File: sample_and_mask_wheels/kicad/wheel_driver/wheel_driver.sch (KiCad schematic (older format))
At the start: 10 parts, among them J1 Screw_Terminal_01x04, J2 Screw_Terminal_01x04, J3 Screw_Terminal_01x04, SW1 SW_Coded_SH-7040

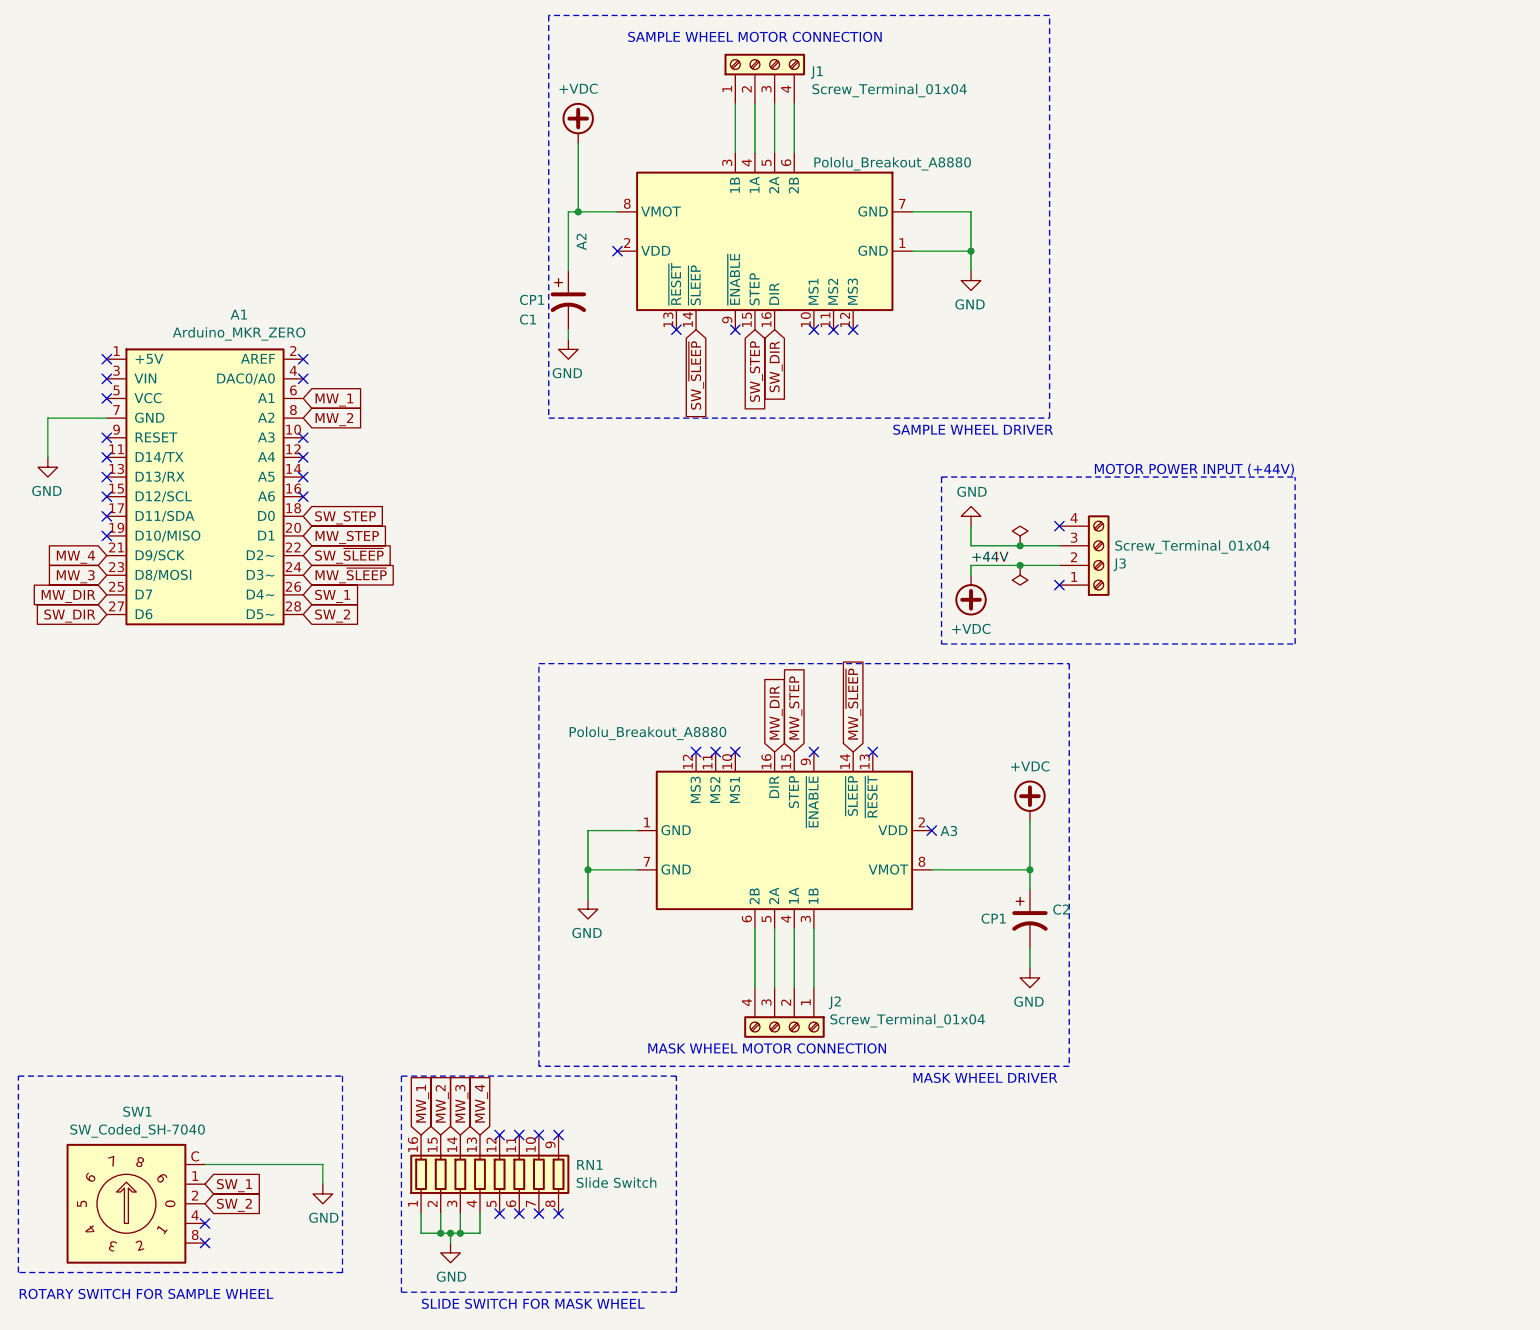
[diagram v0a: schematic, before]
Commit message: add motor connections to schematifc
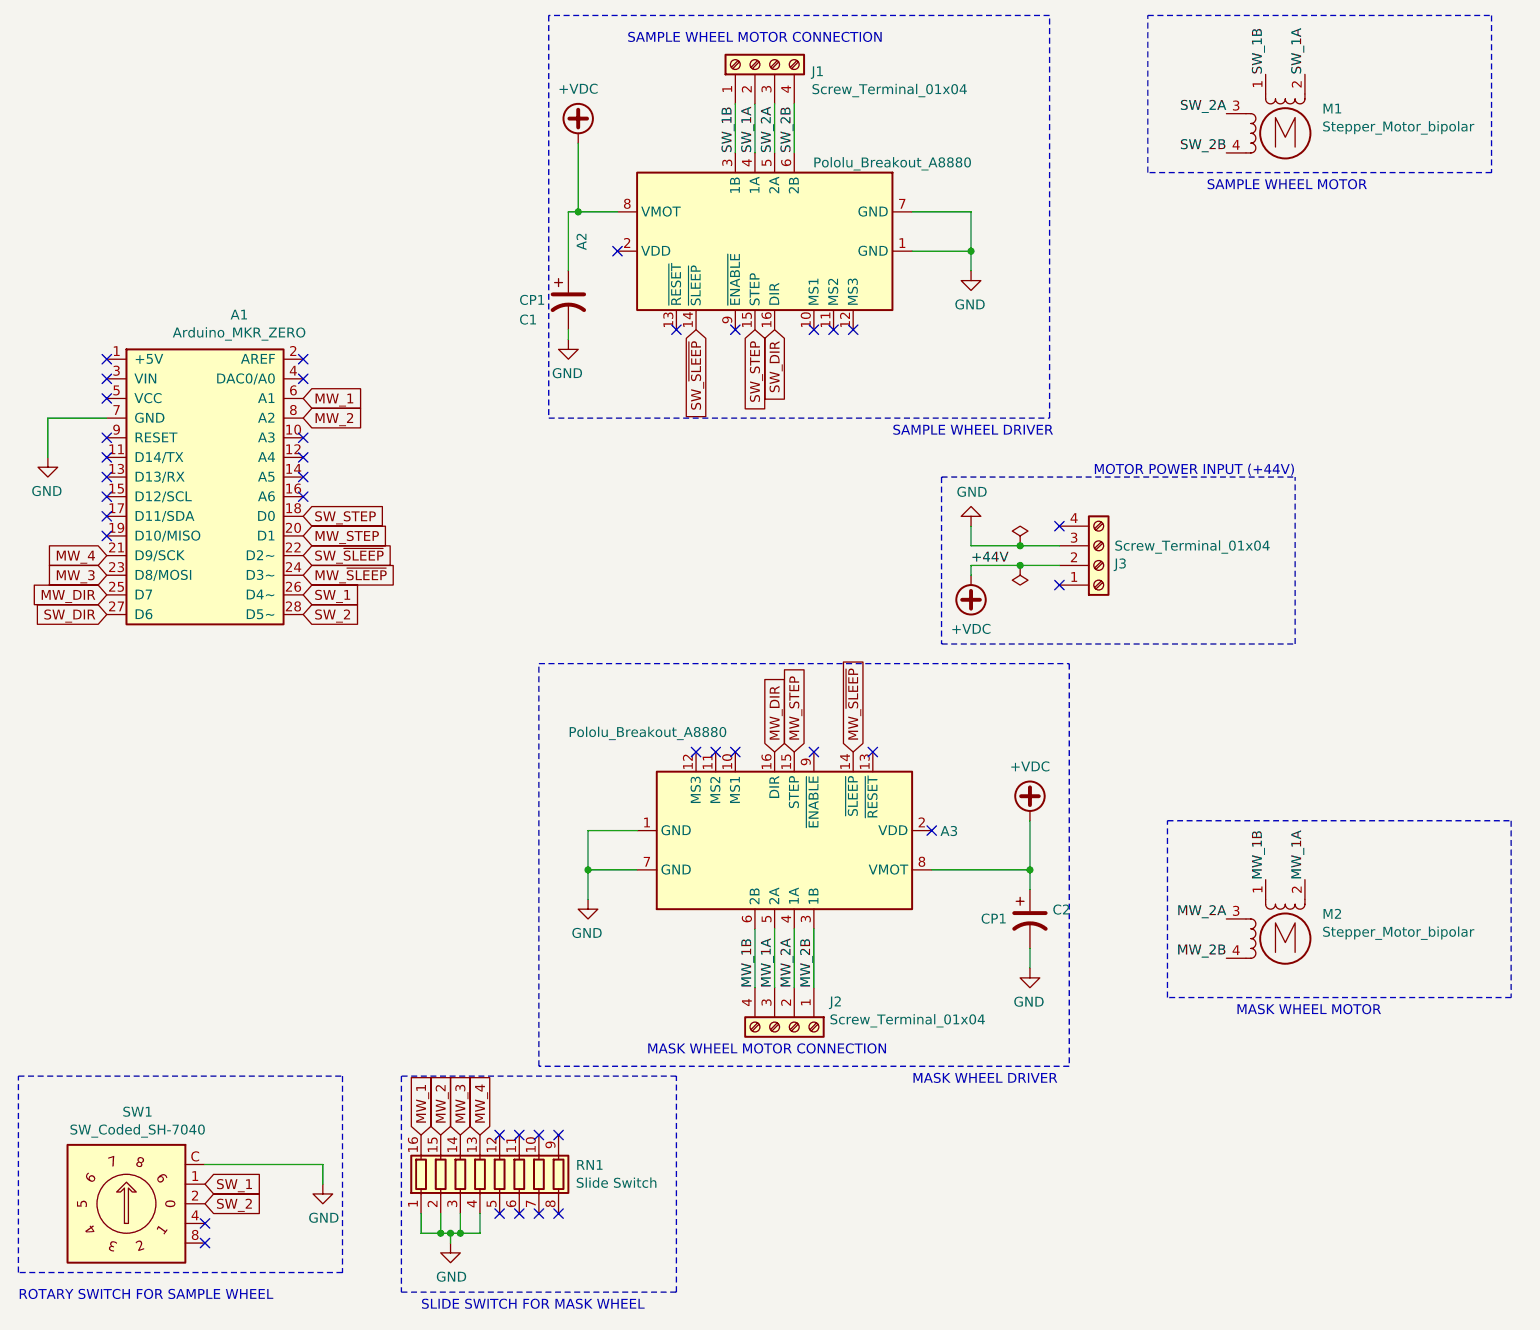
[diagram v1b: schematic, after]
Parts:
- added M1, M2: Stepper_Motor_bipolar, symbol Motor:Stepper_Motor_bipolar
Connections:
- net SW_1B: now reaches A2.3 (1B), J1.1 (Pin_1)
- net SW_1B: now also M1.1
- net SW_1A: now reaches A2.4 (1A), J1.2 (Pin_2)
- net SW_1A: now also M1.2 (-)
- net SW_2A: now reaches A2.5 (2A), J1.3 (Pin_3)
- net SW_2A: now also M1.3
- net SW_2B: now reaches A2.6 (2B), J1.4 (Pin_4)
- net SW_2B: now also M1.4
- net MW_2B: now reaches A3.3 (1B), J2.1 (Pin_1)
- net MW_2B: now also M2.4
- net MW_2A: now reaches A3.4 (1A), J2.2 (Pin_2)
- net MW_2A: now also M2.3
- net MW_1A: now reaches A3.5 (2A), J2.3 (Pin_3)
- net MW_1A: now also M2.2 (-)
- net MW_1B: now reaches A3.6 (2B), J2.4 (Pin_4)
- net MW_1B: now also M2.1
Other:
- note added: "MASK WHEEL MOTOR"
- note added: "SAMPLE WHEEL MOTOR"
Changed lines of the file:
@@
 EESchema Schematic File Version 4
+LIBS:wheel_driver-cache
 EELAYER 29 0
 EELAYER END
@@
 Wire Wire Line
 	6450 3400 6200 3400
+$Comp
+L Motor:Stepper_Motor_bipolar M1
+U 1 1 5BDB3F6A
+P 7800 1200
+F 0 "M1" H 7988 1324 50  0000 L CNN
+F 1 "Stepper_Motor_bipolar" H 7988 1233 50  0000 L CNN
+F 2 "" H 7810 1190 50  0001 C CNN
+F 3 "http://www.infineon.com/dgdl/Application-Note-TLE8110EE_driving_UniPolarStepperMotor_V1.1.pdf?fileId=db3a30431be39b97011be5d0aa0a00b0" H 7810 1190 50  0001 C CNN
+	1    7800 1200
+	1    0    0    -1
+$EndComp
+$Comp
+L Motor:Stepper_Motor_bipolar M2
+U 1 1 5BDB54BA
+P 7800 5300
+F 0 "M2" H 7988 5424 50  0000 L CNN
+F 1 "Stepper_Motor_bipolar" H 7988 5333 50  0000 L CNN
+F 2 "" H 7810 5290 50  0001 C CNN
+F 3 "http://www.infineon.com/dgdl/Application-Note-TLE8110EE_driving_UniPolarStepperMotor_V1.1.pdf?fileId=db3a30431be39b97011be5d0aa0a00b0" H 7810 5290 50  0001 C CNN
+	1    7800 5300
+	1    0    0    -1
+$EndComp
+Text Notes 7550 5700 0    50   ~ 0
+MASK WHEEL MOTOR
+Text Notes 7400 1500 0    50   ~ 0
+SAMPLE WHEEL MOTOR
+Text Label 5300 1300 1    50   ~ 0
+SW_2B
+Text Label 5200 1300 1    50   ~ 0
+SW_2A
+Text Label 5100 1300 1    50   ~ 0
+SW_1A
+Text Label 5000 1300 1    50   ~ 0
+SW_1B
+Text Label 7500 1300 2    50   ~ 0
+SW_2B
+Text Label 7500 1100 2    50   ~ 0
+SW_2A
+Text Label 7700 900  1    50   ~ 0
+SW_1B
+Text Label 7900 900  1    50   ~ 0
+SW_1A
+Wire Notes Line
+	7100 600  8850 600
+Wire Notes Line
+	8850 600  8850 1400
+Wire Notes Line
+	8850 1400 7100 1400
+Wire Notes Line
+	7100 1400 7100 600
+Text Label 5100 5550 1    50   ~ 0
+MW_1B
+Text Label 5200 5550 1    50   ~ 0
+MW_1A
+Text Label 5300 5550 1    50   ~ 0
+MW_2A
+Text Label 5400 5550 1    50   ~ 0
+MW_2B
+Text Label 7700 5000 1    50   ~ 0
+MW_1B
+Text Label 7900 5000 1    50   ~ 0
+MW_1A
+Text Label 7500 5200 2    50   ~ 0
+MW_2A
+Text Label 7500 5400 2    50   ~ 0
+MW_2B
+Wire Notes Line
+	7200 5600 7200 4700
+Wire Notes Line
+	7200 4700 8950 4700
+Wire Notes Line
+	8950 4700 8950 5600
+Wire Notes Line
+	8950 5600 7200 5600
 $EndSCHEMATC

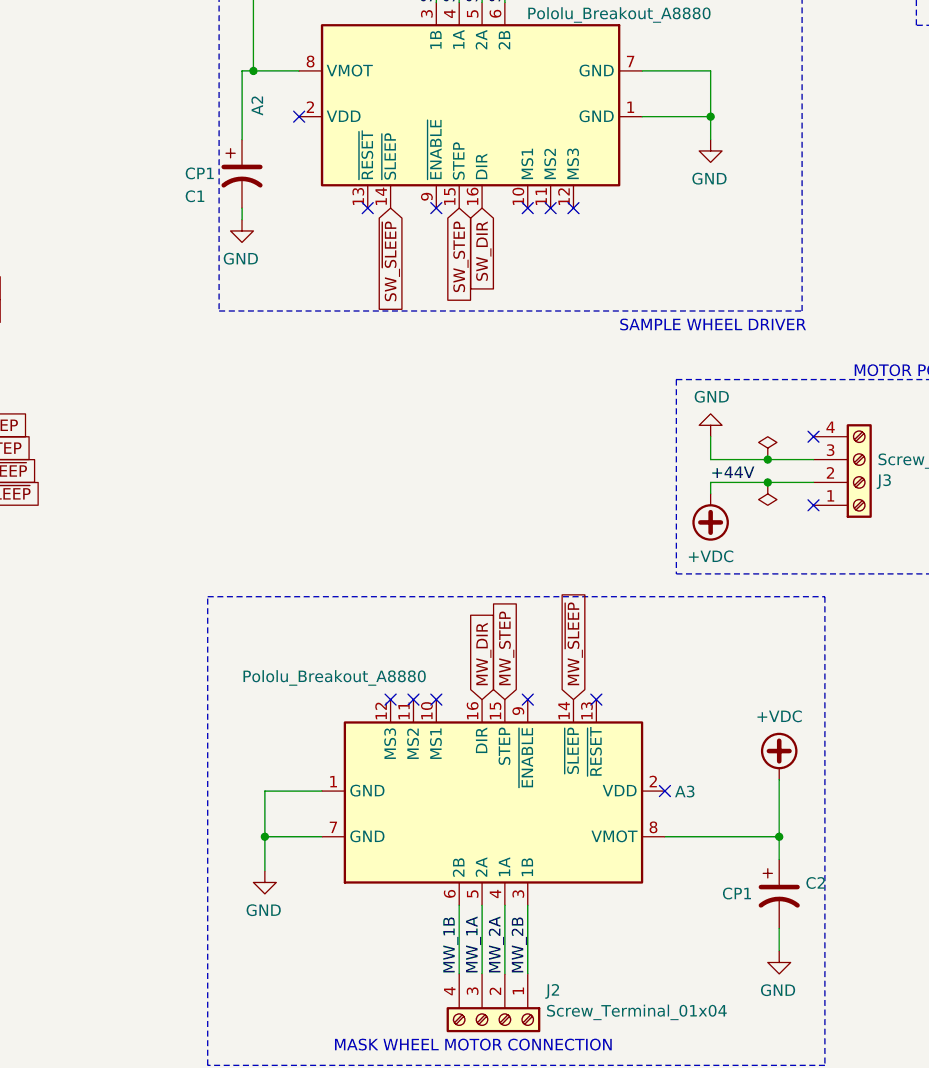
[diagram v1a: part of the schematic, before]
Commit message: fix cap value in schemtaic
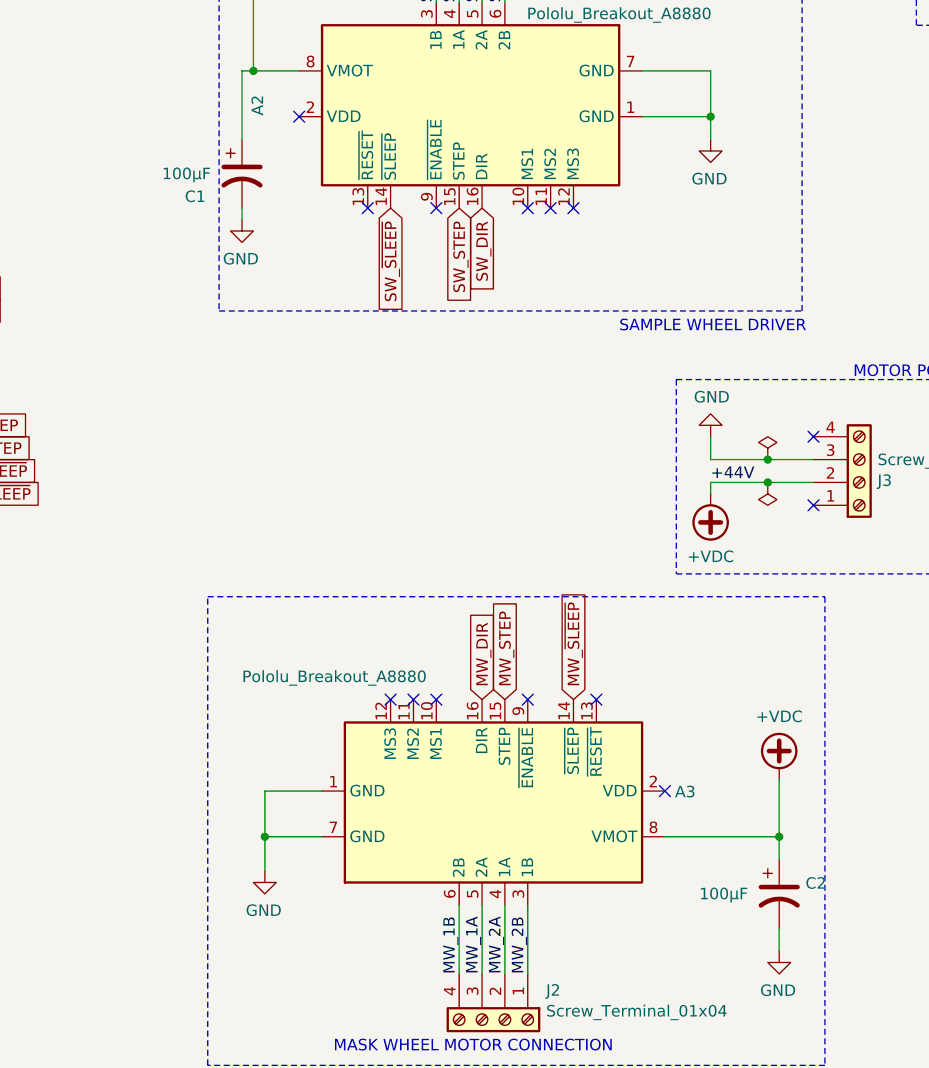
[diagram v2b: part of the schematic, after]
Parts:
- C1, C2: value CP1 -> 100μF
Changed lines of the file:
@@
 P 4150 2050
 F 0 "C1" H 3900 1950 50  0000 L CNN
-F 1 "CP1" H 3900 2050 50  0000 L CNN
+F 1 "100μF" H 3800 2050 50  0000 L CNN
 F 2 "" H 4150 2050 50  0001 C CNN
 F 3 "~" H 4150 2050 50  0001 C CNN
@@
 P 6500 5200
 F 0 "C2" H 6615 5246 50  0000 L CNN
-F 1 "CP1" H 6250 5200 50  0000 L CNN
+F 1 "100μF" H 6150 5200 50  0000 L CNN
 F 2 "" H 6500 5200 50  0001 C CNN
 F 3 "~" H 6500 5200 50  0001 C CNN

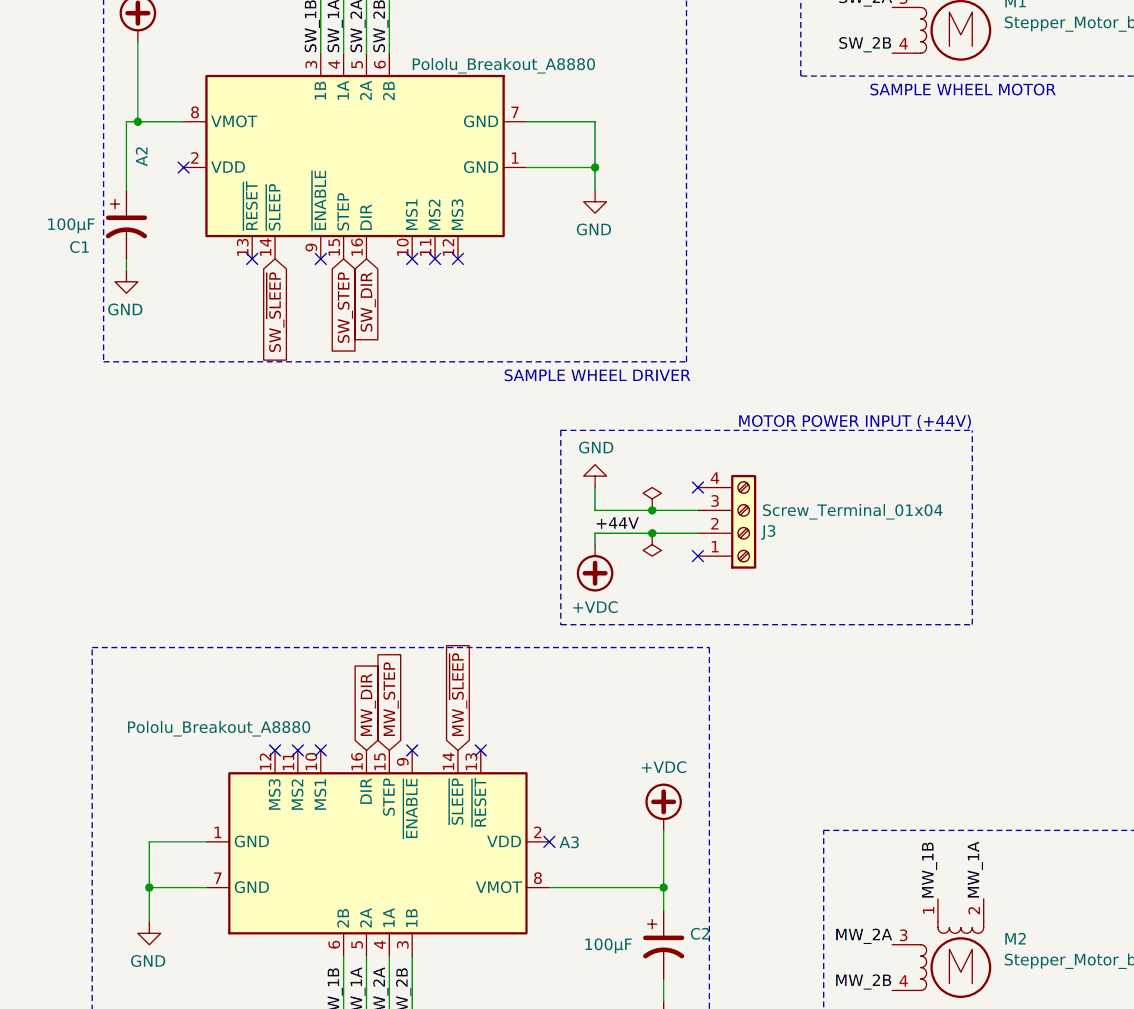
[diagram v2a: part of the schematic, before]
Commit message: change scematic to +12v input
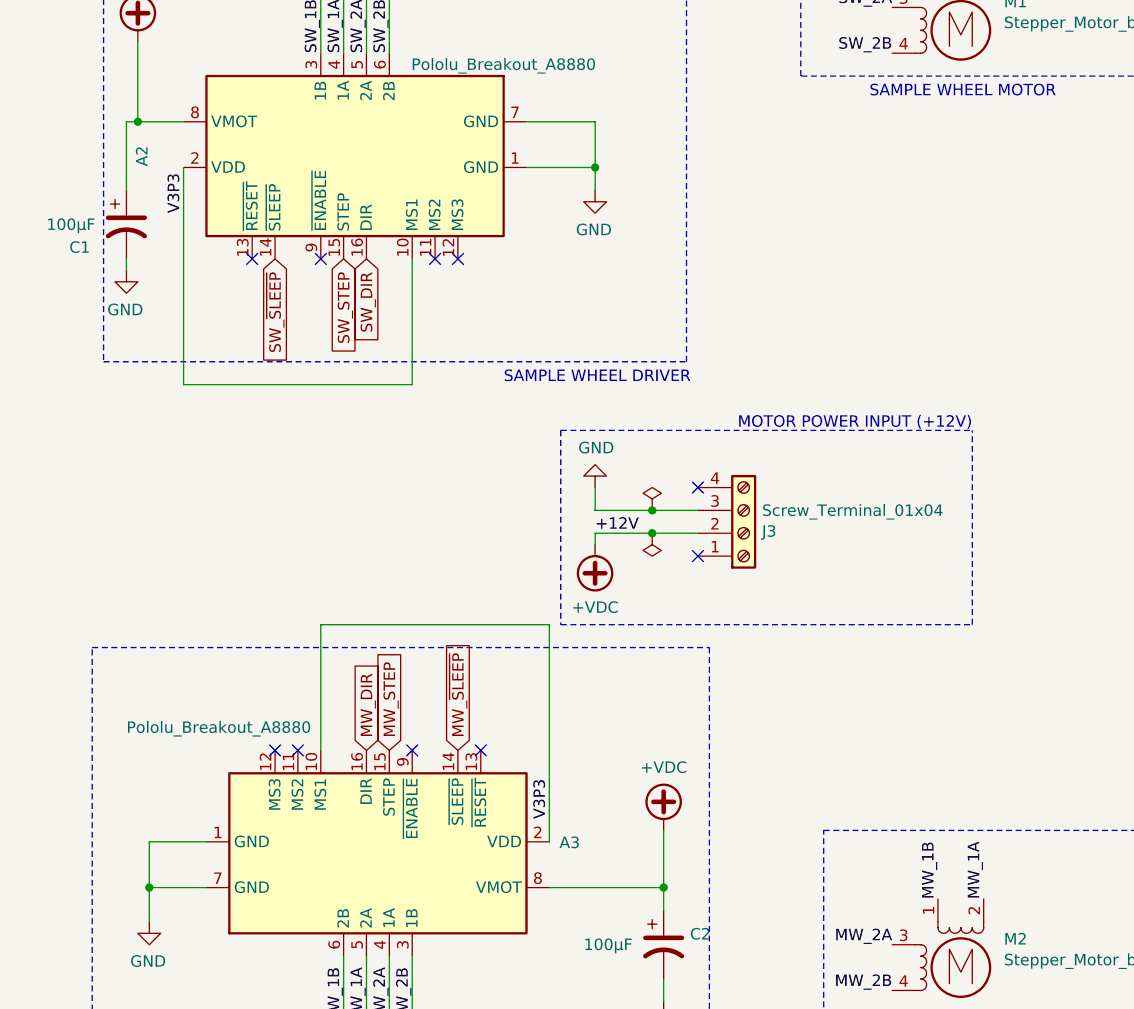
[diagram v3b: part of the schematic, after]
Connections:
- net V3P3: now reaches A2.10 (MS1)
- net V3P3: now also A2.2 (VDD), A3.10 (MS1), A3.2 (VDD)
- no-connect marks 39 -> 35
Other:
- note added: "MOTOR POWER INPUT (+12V)"
- note removed: "MOTOR POWER INPUT (+44V)"
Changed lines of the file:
@@
 $EndComp
 Text Notes 7850 2950 2    50   ~ 0
-MOTOR POWER INPUT (+44V)
+MOTOR POWER INPUT (+12V)
 NoConn ~ 6650 3200
 NoConn ~ 6650 3500
@@
 	6200 3400 6200 3450
 Text Label 6200 3400 0    50   ~ 0
-+44V
++12V
 Wire Notes Line
 	3000 6000 3000 7000
@@
 NoConn ~ 5000 2200
 NoConn ~ 4700 2200
-NoConn ~ 5400 2200
 NoConn ~ 5500 2200
 NoConn ~ 5600 2200
-NoConn ~ 6000 4750
-NoConn ~ 4400 1800
 NoConn ~ 4800 4350
 NoConn ~ 4900 4350
-NoConn ~ 5000 4350
 NoConn ~ 5400 4350
 NoConn ~ 5700 4350
@@
 Wire Notes Line
 	8950 5600 7200 5600
+Wire Wire Line
+	6000 4750 6000 3800
+Wire Wire Line
+	6000 3800 5000 3800
+Wire Wire Line
+	5000 3800 5000 4350
+Wire Wire Line
+	5400 2200 5400 2750
+Wire Wire Line
+	5400 2750 4400 2750
+Wire Wire Line
+	4400 2750 4400 1800
+Text Label 4400 2000 1    50   ~ 0
+V3P3
+Text Label 6000 4650 1    50   ~ 0
+V3P3
 $EndSCHEMATC
